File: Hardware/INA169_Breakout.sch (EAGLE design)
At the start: 19 parts, among them U1 INA169

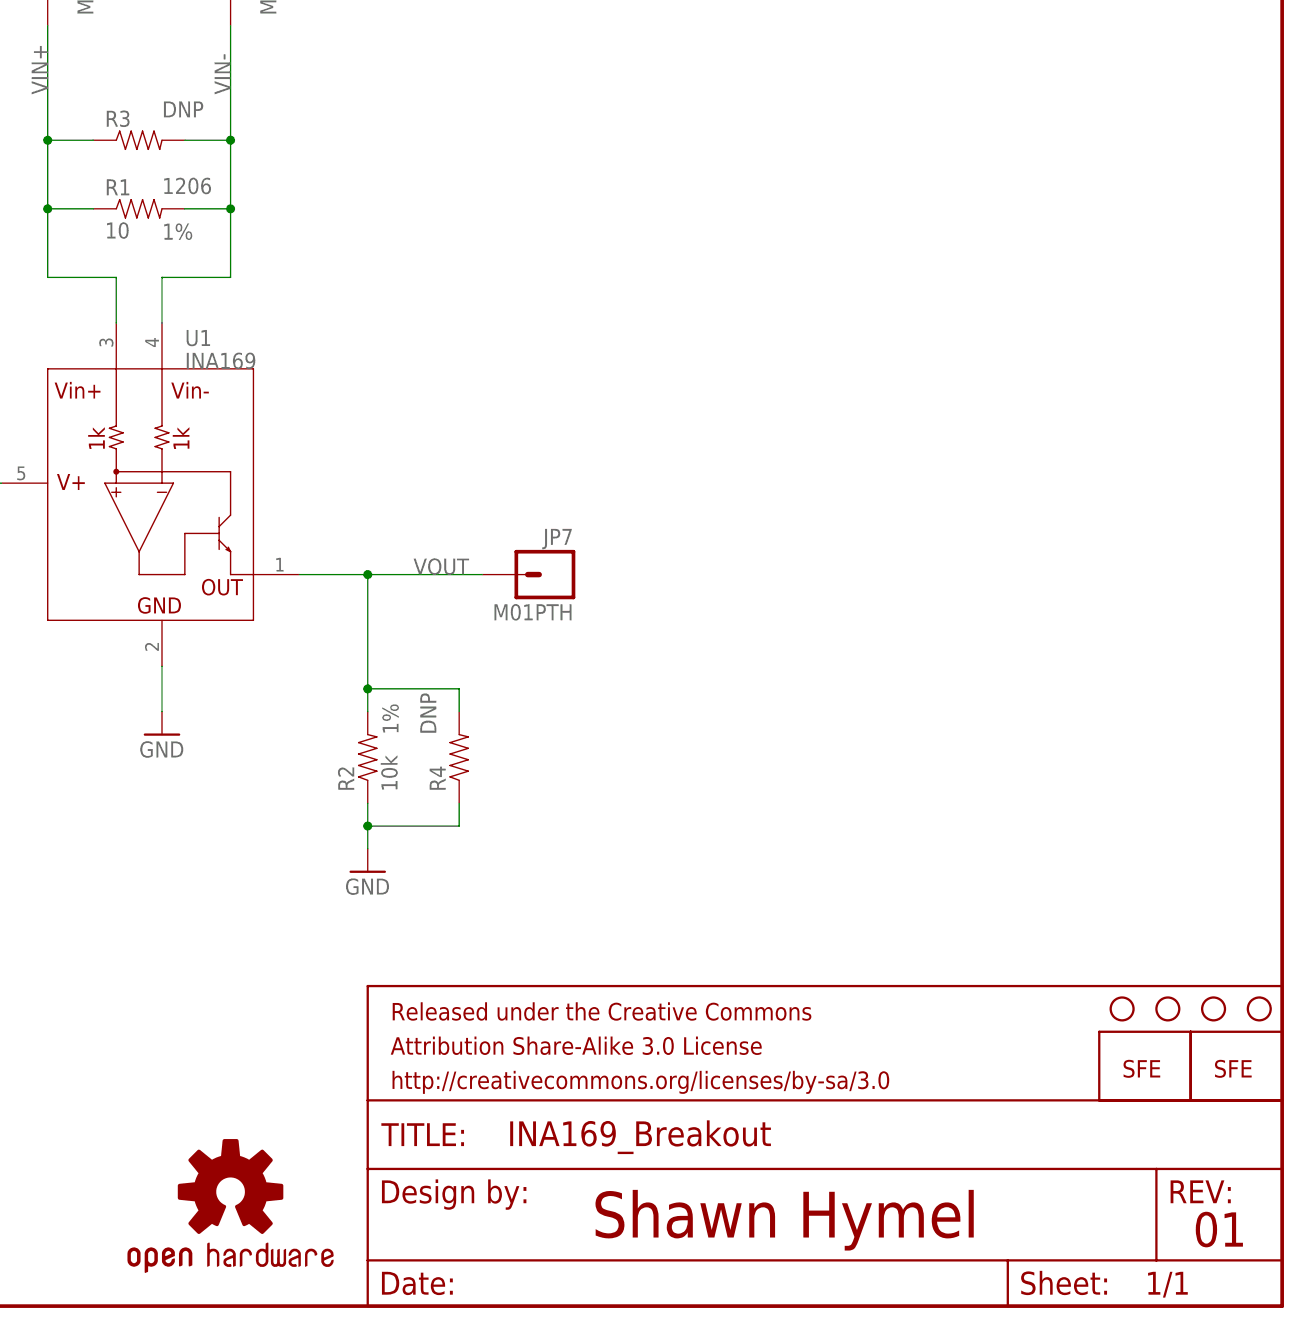
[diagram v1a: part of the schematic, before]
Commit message: Fixed silkscreen. Ready for review.
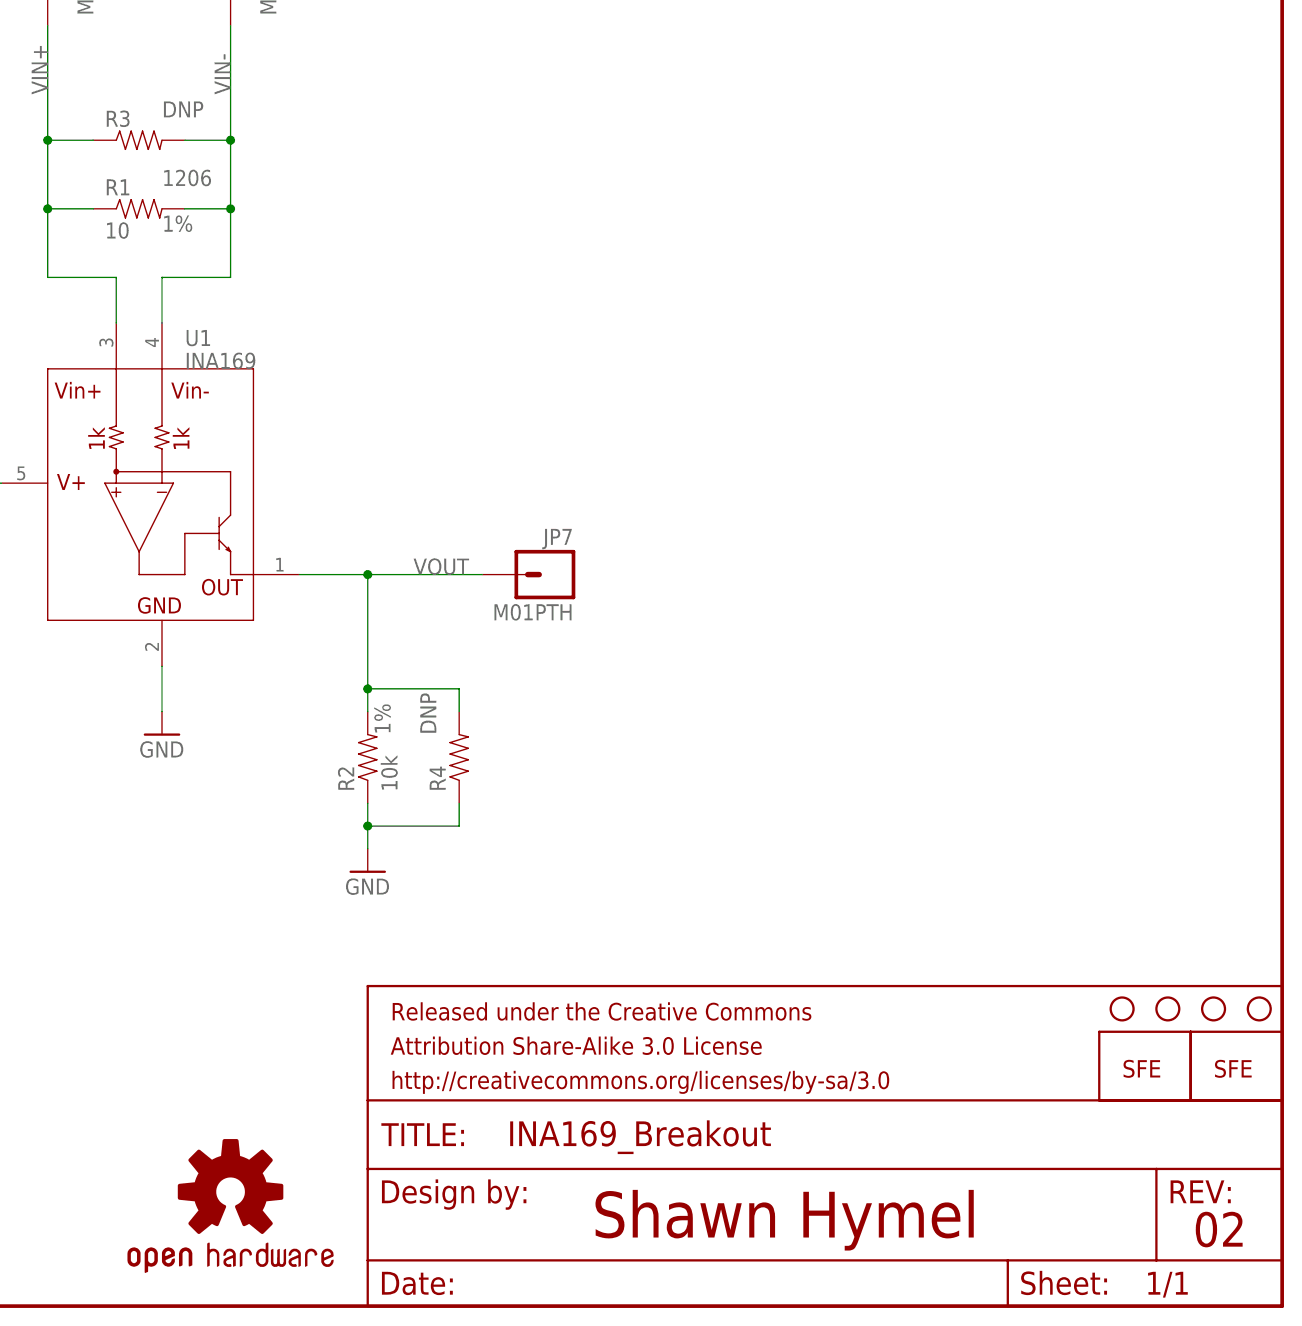
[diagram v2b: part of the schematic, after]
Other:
- note added: "02"
- note removed: "01"
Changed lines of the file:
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@@
 <plain>
 <text x="172.212" y="7.62" size="5.08" layer="94">Shawn Hymel</text>
-<text x="239.014" y="6.604" size="3.81" layer="94">01</text>
+<text x="239.014" y="6.604" size="3.81" layer="94">02</text>
 </plain>
 <instances>
@@
 </instance>
 <instance part="R2" gate="G$1" x="147.32" y="60.96" rot="R90">
-<attribute name="TOL" x="149.86" y="63.5" size="1.778" layer="96" rot="R90" align="center-left"/>
+<attribute name="TOL" x="149.86" y="63.5" size="1.778" layer="96" rot="R90"/>
 </instance>
 <instance part="R1" gate="G$1" x="121.92" y="121.92">
-<attribute name="SIZE" x="124.46" y="124.46" size="1.778" layer="96" align="center-left"/>
-<attribute name="TOL" x="124.46" y="119.38" size="1.778" layer="96" align="center-left"/>
+<attribute name="SIZE" x="124.46" y="124.46" size="1.778" layer="96"/>
+<attribute name="TOL" x="124.46" y="119.38" size="1.778" layer="96"/>
 </instance>
 </instances>

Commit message: Added tables on sch, added pads on brd
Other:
- note added: "(Vin+, Vin-)"
- note added: "-0.3V to 75V"
- note added: "0.1Ω"
- note added: "10"
- note added: "10Ω"
- note added: "1Ω"
- note added: "3.5mA - 35mA"
- note added: "350mA - 3.5A"
- note added: "35mA - 350mA"
- note added: "Common Mode"
- note added: "Current Sense"
- note added: "For VCC = 5V"
- note added: "IS"
- note added: "RL"
- note added: "RS"
- note added: "Range"
- note added: "VCC"
- note added: "VOUT = IS x RS x RL / 1kΩ"
- note added: "Voltage Limits"
- note removed: "02"
- moved on the sheet: C1, JP1, JP2, JP5, JP6, JP7, R1, R2, R3, R4, U1

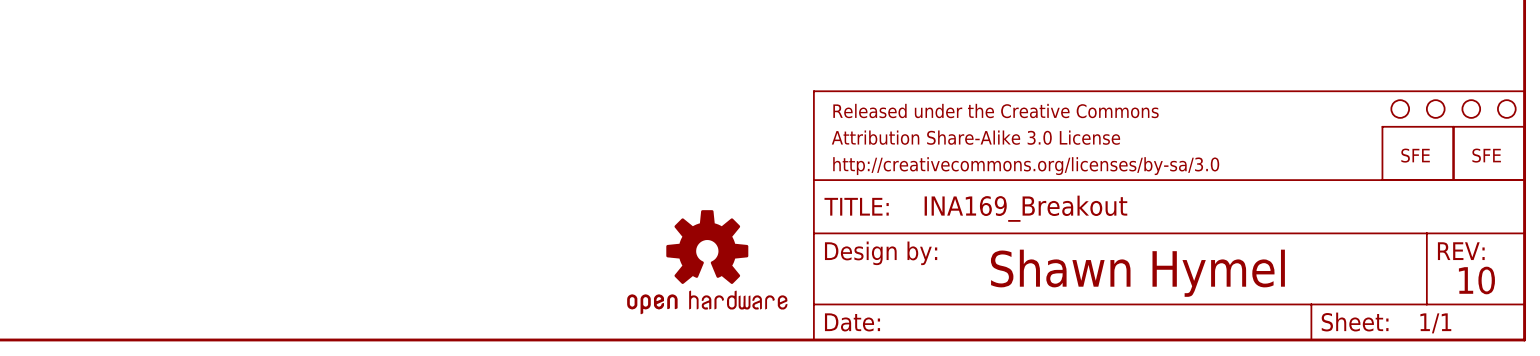
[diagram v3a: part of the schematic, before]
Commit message: Changed to smaller SFE logo on brd
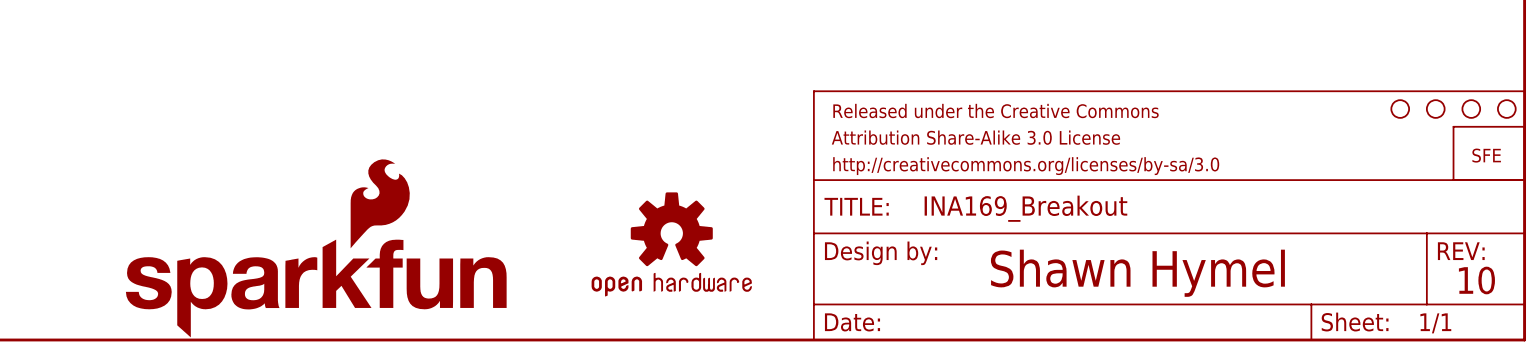
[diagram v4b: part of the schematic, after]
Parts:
- LOGO1: value LOGO-SFENEW -> SFE_LOGO_NAME_FLAME.1_INCH; device SparkFun-Aesthetics:LOGO-SFENEW -> SparkFun-Aesthetics:SFE_LOGO_NAME_FLAME.1_INCH
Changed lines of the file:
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@@
 <setting verticaltext="up"/>
 </settings>
-<grid distance="0.1" unitdist="inch" unit="inch" style="lines" multiple="1" display="no" altdistance="0.01" altunitdist="inch" altunit="inch"/>
+<grid distance="0.1" unitdist="inch" unit="inch" style="lines" multiple="1" display="yes" altdistance="0.01" altunitdist="inch" altunit="inch"/>
 <layers>
 <layer number="1" name="Top" color="4" fill="1" visible="no" active="no"/>
@@
 <part name="STANDOFF3" library="SparkFun-Electromechanical" deviceset="STAND-OFF" device=""/>
 <part name="STANDOFF4" library="SparkFun-Electromechanical" deviceset="STAND-OFF" device=""/>
-<part name="LOGO1" library="SparkFun-Aesthetics" deviceset="LOGO-SFE" device="NEW"/>
+<part name="LOGO1" library="SparkFun-Aesthetics" deviceset="SFE_LOGO_NAME_FLAME" device=".1_INCH"/>
 <part name="LOGO2" library="SparkFun-Aesthetics" deviceset="OSHW-LOGO" device="S"/>
 <part name="LOGO3" library="SparkFun-Aesthetics" deviceset="LOGO-SFE" device="SK"/>
@@
 <instance part="STANDOFF3" gate="G$1" x="236.22" y="33.02"/>
 <instance part="STANDOFF4" gate="G$1" x="231.14" y="33.02"/>
-<instance part="LOGO1" gate="G$1" x="241.3" y="25.4"/>
-<instance part="LOGO2" gate="G$1" x="132.08" y="12.7"/>
-<instance part="LOGO3" gate="G$1" x="231.14" y="25.4"/>
+<instance part="LOGO1" gate="G$1" x="48.26" y="0"/>
+<instance part="LOGO2" gate="G$1" x="127" y="15.24"/>
+<instance part="LOGO3" gate="G$1" x="241.3" y="25.4"/>
 <instance part="GND1" gate="1" x="50.8" y="78.74"/>
 <instance part="GND2" gate="1" x="66.04" y="78.74"/>
